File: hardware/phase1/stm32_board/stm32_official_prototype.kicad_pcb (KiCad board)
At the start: 6 copper layers, 103.6 x 114 mm, 73 parts, among them CN11 Conn_02x36_Odd_Even, CN12 Conn_02x36_Odd_Even, CN14 USB_B_Micro, CN5 Conn_ARM_JTAG_SWD_10, J1 Screw_Terminal_01x02, T2 9013, U11 STM32L496ZGTx, U12 STMPS2151STR, U13 USBLC6-2SC6, U6 LD39050PU33R, U8 TSV631AILT, U9 ESDALC6V1W5

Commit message: "idk whats the final anymore" stm32 board (2.22.25)
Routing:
- net GND: track 200.0 -> 240.2 mm, vias 61 -> 64
- net PC3: track 74.6 -> 73.2 mm
- added copper zone on In2.Cu, net GND
- added copper zone on In1.Cu, net VDD
- removed copper zone on In4.Cu, net GND
- removed copper zone on In3.Cu, net VDD
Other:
- copper layers 6 -> 4
- board text added: "+3V3"

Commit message: Update STM board
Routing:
- net GND: track 240.2 -> 286.6 mm, vias 64 -> 79

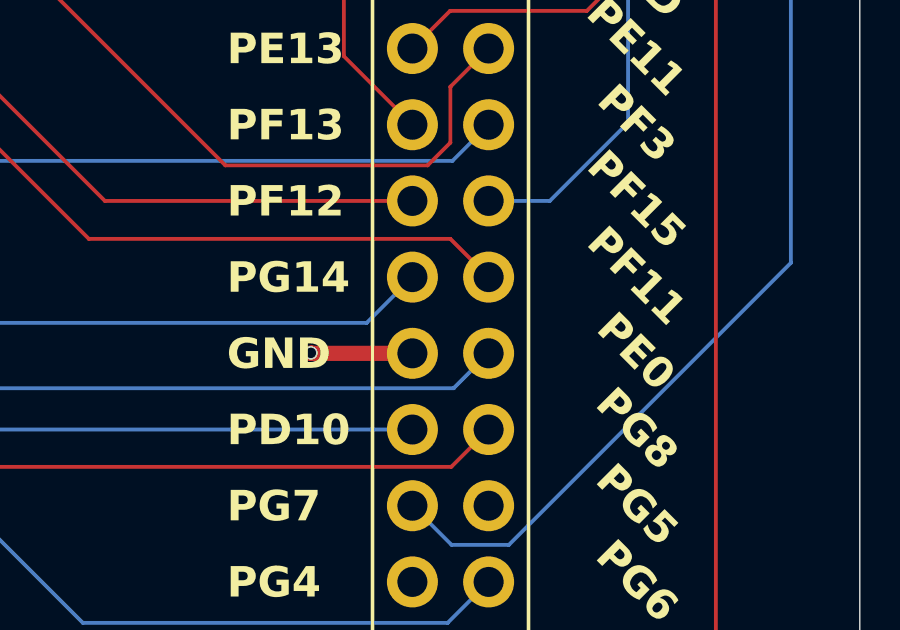
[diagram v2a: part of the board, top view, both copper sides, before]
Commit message: Fix STM floating gnd
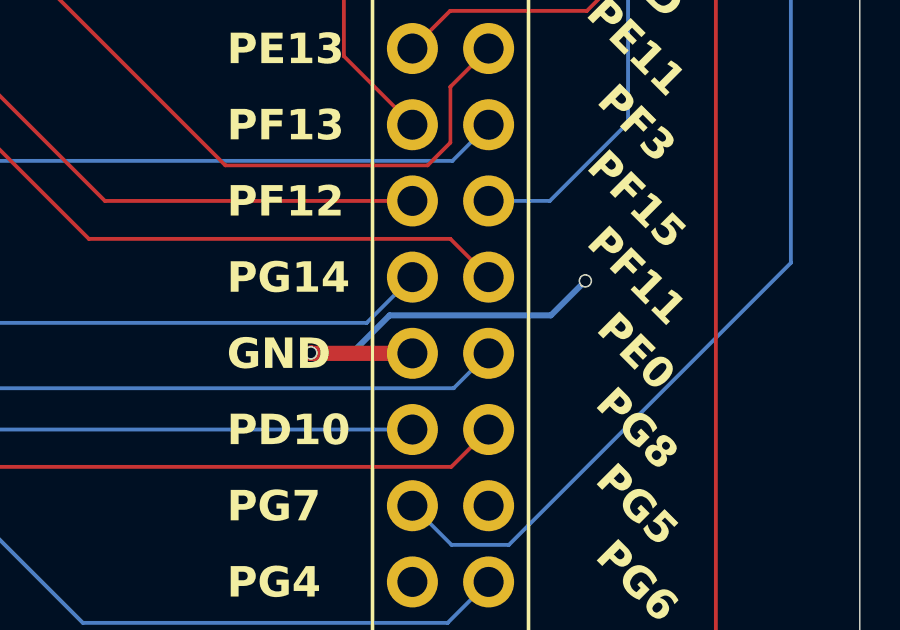
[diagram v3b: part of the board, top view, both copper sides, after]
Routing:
- net GND: track 286.6 -> 296.8 mm, vias 79 -> 80
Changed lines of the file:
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@@
+	)
+	(via
+		(at 173.75 114.6)
+		(size 0.45)
+		(drill 0.35)
+		(layers "F.Cu" "B.Cu")
+		(free yes)
+		(net 130)
 	)
 	(via
@@
 	)
 	(segment
+		(start 165.973715 117)
+		(end 164.6 117)
+		(width 0.2)
+		(layer "B.Cu")
+		(net 130)
+	)
+	(segment
 		(start 143.8 63.65)
 		(end 142.15 65.3)
@@
 	)
 	(segment
+		(start 167.223715 115.75)
+		(end 165.973715 117)
+		(width 0.2)
+		(layer "B.Cu")
+		(net 130)
+	)
+	(segment
 		(start 92 63.675)
 		(end 94.375 63.675)
@@
 	)
 	(segment
+		(start 172.6 115.75)
+		(end 167.223715 115.75)
+		(width 0.2)
+		(layer "B.Cu")
+		(net 130)
+	)
+	(segment
 		(start 170.524648 76.375)
 		(end 171.125 76.375)
@@
 		(layer "B.Cu")
 		(net 130)
+	)
+	(segment
+		(start 173.75 114.6)
+		(end 172.6 115.75)
+		(width 0.2)
+		(layer "B.Cu")
+		(net 130)
